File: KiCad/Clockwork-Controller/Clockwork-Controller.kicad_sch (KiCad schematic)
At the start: 98 parts, among them CN2 PJ-307N5, J1 DIN-6 male, J2 to DIN-6 Male, J3 Pause Button, J4 ICSP, J5 LED-Connector, J6 FTDI, Q1 AO3400A, Q2 SS8050, Q3 SS8050, Q4 SS8050, SW1 Guide/Follow, SW2 Mode -, SW3 Mode +, SW4 Frame -, SW5 Frame +, U1 ECS-TXO-3225MV-160-TR, U2 AP2210N-3.3TRG1, U3 74HCT14, U4 G3VM-61VY3(TR), U5 MCP4725, U6 LMC6482, U7 ATmega328P-A

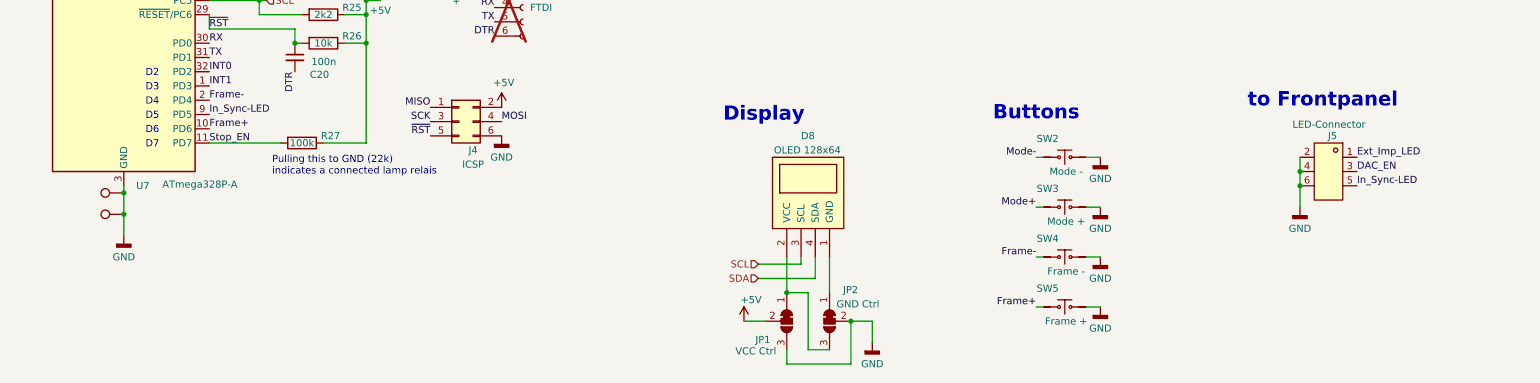
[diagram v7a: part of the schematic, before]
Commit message: Adjusting LED-Pins on the Controller Side (adding VCC)
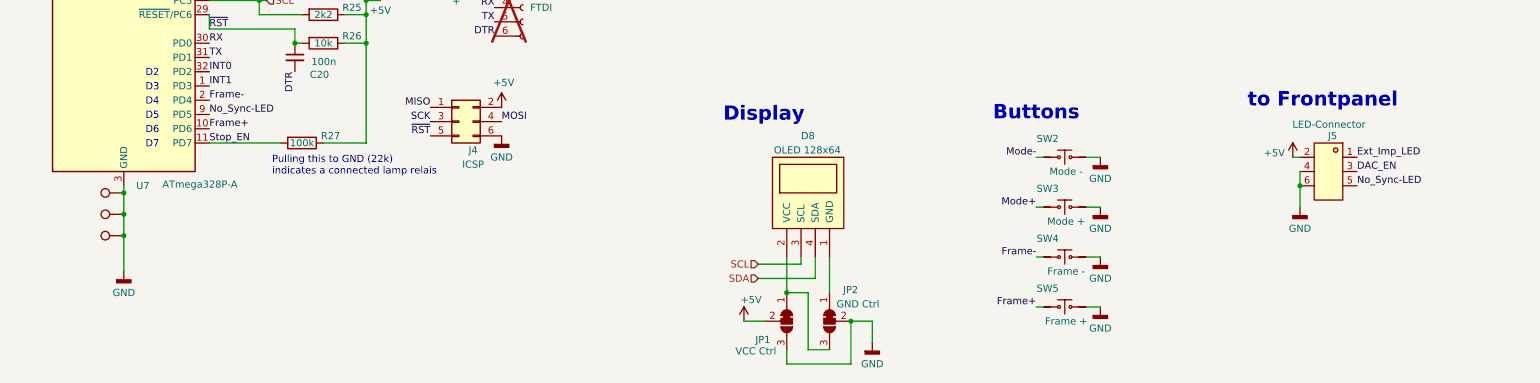
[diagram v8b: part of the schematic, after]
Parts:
- added TP12: GND, TestPoint:TestPoint_THTPad_1.5x1.5mm_Drill0.7mm, symbol Peacemans Teile:TestPoint_named
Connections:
- net +5V: now also J5.2
- net GND: now also TP12.1; no longer J5.2
- net In_Sync-LED renamed No_Sync-LED
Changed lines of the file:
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@@
 	)
 	(junction
+		(at 63.5 254)
+		(diameter 0)
+		(color 0 0 0 0)
+	)
+	(junction
 		(at 123.19 52.07)
 		(diameter 0)
@@
 	)
 	(junction
-		(at 273.05 242.57)
-		(diameter 0)
-		(color 0 0 0 0)
-	)
-	(junction
 		(at 334.01 72.39)
 		(diameter 0)
@@
 	(wire
 		(pts
+			(xy 63.5 254) (xy 63.5 260.35)
+		)
+		(stroke
+			(width 0)
+			(type default)
+		)
+	)
+	(wire
+		(pts
 			(xy 361.95 71.12) (xy 365.76 71.12)
 		)
@@
 	(wire
 		(pts
+			(xy 271.78 240.03) (xy 273.05 240.03)
+		)
+		(stroke
+			(width 0)
+			(type default)
+		)
+	)
+	(wire
+		(pts
 			(xy 128.27 208.28) (xy 128.27 205.74)
 		)
@@
 	(wire
 		(pts
-			(xy 273.05 240.03) (xy 273.05 242.57)
-		)
-		(stroke
-			(width 0)
-			(type default)
-		)
-	)
-	(wire
-		(pts
 			(xy 99.06 237.49) (xy 106.68 237.49)
 		)
@@
 		)
 	)
-	(label "In_Sync-LED"
+	(label "No_Sync-LED"
 		(at 78.74 232.41 0)
 		(effects
@@
 		)
 	)
-	(label "In_Sync-LED"
+	(label "No_Sync-LED"
 		(at 283.21 245.11 0)
 		(effects
@@
 	)
 	(symbol
+		(lib_id "Peacemans Teile:TestPoint_named")
+		(at 63.5 254 90)
+		(unit 1)
+		(exclude_from_sim no)
+		(in_bom yes)
+		(on_board yes)
+		(dnp no)
+		(fields_autoplaced yes)
+		(property "Reference" "TP12"
+			(at 56.642 254 0)
+			(effects
+				(font
+					(size 1.27 1.27)
+				)
+				(hide yes)
+			)
+		)
+		(property "Value" "GND"
+			(at 58.42 254 0)
+			(effects
+				(font
+					(size 1.27 1.27)
+				)
+				(hide yes)
+			)
+		)
+		(property "Footprint" "TestPoint:TestPoint_THTPad_1.5x1.5mm_Drill0.7mm"
+			(at 63.5 248.92 0)
+			(effects
+				(font
+					(size 1.27 1.27)
+				)
+				(hide yes)
+			)
+		)
+		(property "Datasheet" "~"
+			(at 63.5 248.92 0)
+			(effects
+				(font
+					(size 1.27 1.27)
+				)
+				(hide yes)
+			)
+		)
+		(property "Description" "test point"
+			(at 63.5 254 0)
+			(effects
+				(font
+					(size 1.27 1.27)
+				)
+				(hide yes)
+			)
+		)
+		(property "TP_Label" ""
+			(at 63.5 254 0)
+			(effects
+				(font
+					(size 1.27 1.27)
+				)
+			)
+		)
+		(pin "1"
+		)
+		(instances
+			(project "Clockwork-Controller"
+				(path "/904e3c46-2ed3-4778-9ca9-733b218304b0"
+					(reference "TP12")
+					(unit 1)
+				)
+			)
+		)
+	)
+	(symbol
 		(lib_id "easyEDA:XYC-IRA4335A65-X4")
 		(at 359.41 71.12 180)
@@
 	)
 	(symbol
+		(lib_id "power:+5V")
+		(at 271.78 240.03 0)
+		(unit 1)
+		(exclude_from_sim no)
+		(in_bom yes)
+		(on_board yes)
+		(dnp no)
+		(property "Reference" "#PWR052"
+			(at 271.78 243.84 0)
+			(effects
+				(font
+					(size 1.27 1.27)
+				)
+				(hide yes)
+			)
+		)
+		(property "Value" "+5V"
+			(at 268.478 239.268 0)
+			(effects
+				(font
+					(size 1.27 1.27)
+				)
+			)
+		)
+		(property "Footprint" ""
+			(at 271.78 240.03 0)
+			(effects
+				(font
+					(size 1.27 1.27)
+				)
+				(hide yes)
+			)
+		)
+		(property "Datasheet" ""
+			(at 271.78 240.03 0)
+			(effects
+				(font
+					(size 1.27 1.27)
+				)
+				(hide yes)
+			)
+		)
+		(property "Description" "Power symbol creates a global label with name \"+5V\""
+			(at 271.78 240.03 0)
+			(effects
+				(font
+					(size 1.27 1.27)
+				)
+				(hide yes)
+			)
+		)
+		(pin "1"
+		)
+		(instances
+			(project "Clockwork-Controller"
+				(path "/904e3c46-2ed3-4778-9ca9-733b218304b0"
+					(reference "#PWR052")
+					(unit 1)
+				)
+			)
+		)
+	)
+	(symbol
 		(lib_id "Device:R")
 		(at 99.06 219.71 270)
@@
 	(symbol
 		(lib_id "power:GNDD")
-		(at 63.5 254 0)
+		(at 63.5 260.35 0)
 		(unit 1)
 		(exclude_from_sim no)
@@
 		(dnp no)
 		(property "Reference" "#PWR042"
-			(at 63.5 260.35 0)
+			(at 63.5 266.7 0)
 			(effects
 				(font
@@
 		)
 		(property "Value" "GND"
-			(at 63.5 257.81 0)
+			(at 63.5 264.16 0)
 			(effects
 				(font
@@
 		)
 		(property "Footprint" ""
-			(at 63.5 254 0)
+			(at 63.5 260.35 0)
 			(effects
 				(font
@@
 		)
 		(property "Datasheet" ""
-			(at 63.5 254 0)
+			(at 63.5 260.35 0)
 			(effects
 				(font
@@
 		)
 		(property "Description" "Power symbol creates a global label with name \"GNDD\" , digital ground"
-			(at 63.5 254 0)
+			(at 63.5 260.35 0)
 			(effects
 				(font
